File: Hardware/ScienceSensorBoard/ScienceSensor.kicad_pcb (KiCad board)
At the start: 2 copper layers, 96.5 x 94.5 mm, 70 parts, among them J1 RJ45_LED_Shielded, J2 Conn_02x03_Counter_Clockwise, Q1 BSS138, Q2 BSS138, Q3 BSS138, Q4 BSS138, Q5 BSS138, Q6 BSS138, Q7 BSS138, U1 TSR_1-2450, U2 Teensy4.1_DEV-16771

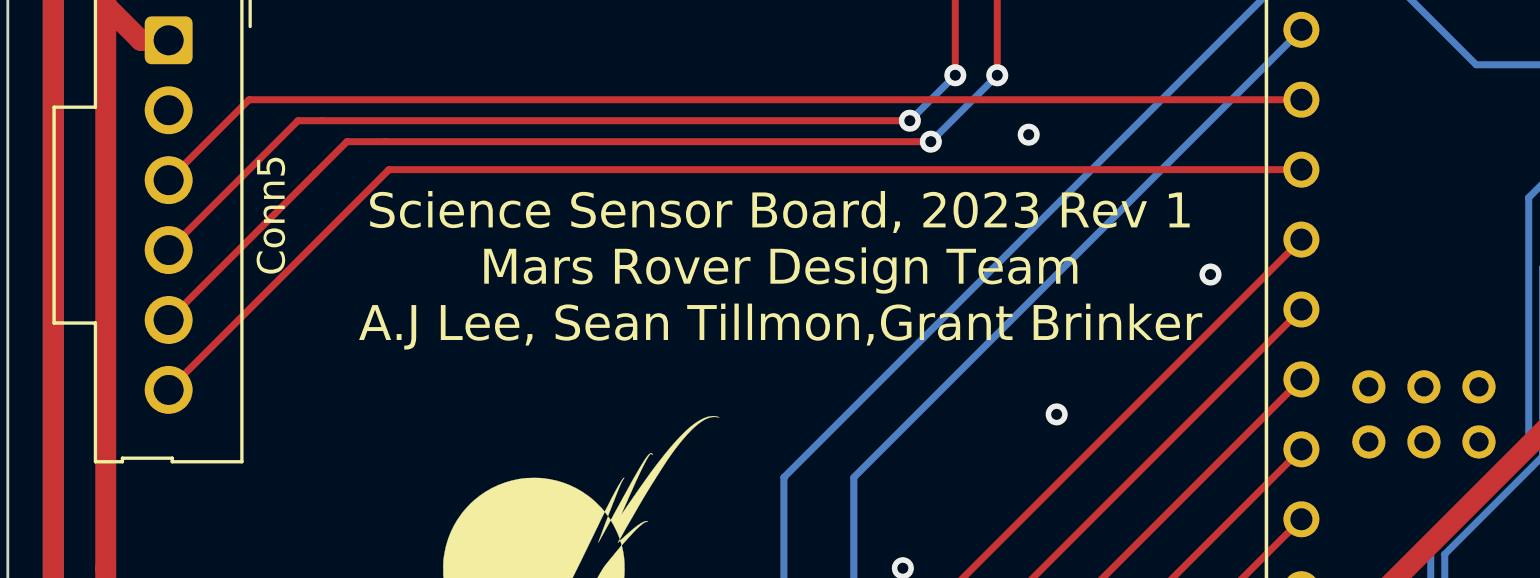
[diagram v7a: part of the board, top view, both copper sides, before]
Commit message: Cleaned up silkscreens
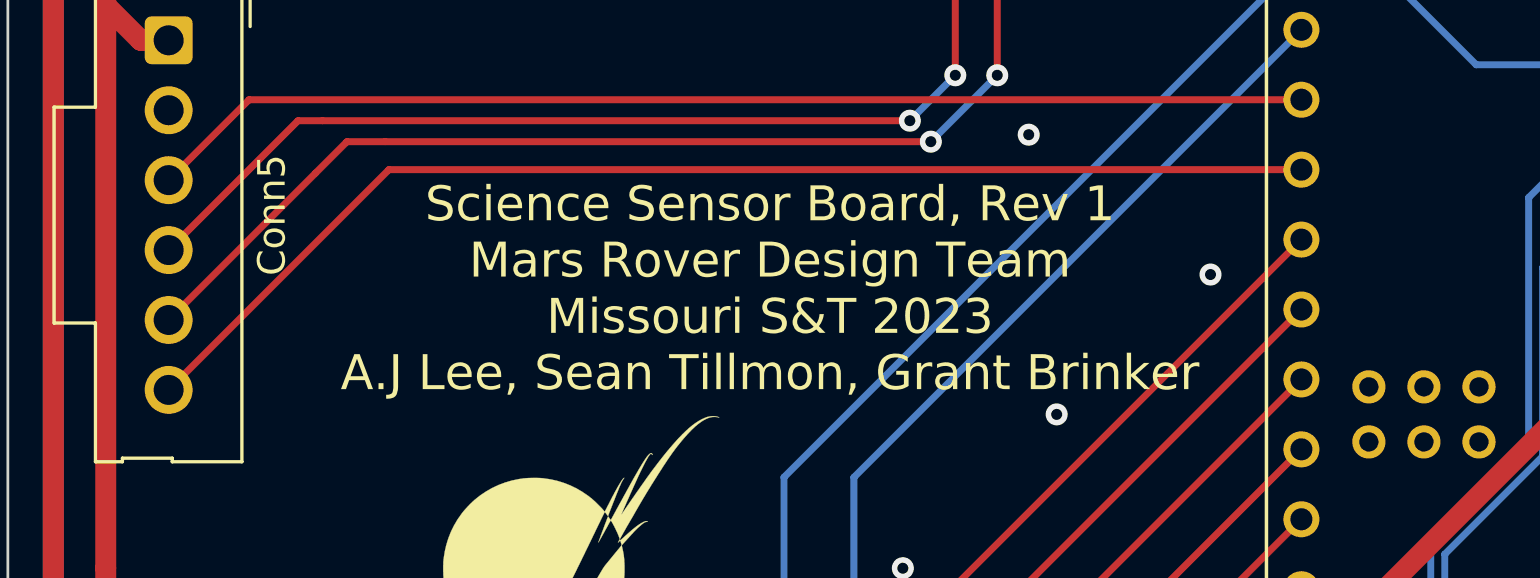
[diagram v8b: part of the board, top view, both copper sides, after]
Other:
- board text added: "Science Sensor Board, Rev 1 Mars Rover Design Team Missouri S&T 2023 A.J Lee, Sean Tillmon, Grant Brinker"
- board text removed: "Science Sensor Board, 2023 Rev 1 Mars Rover Design Team A.J Lee, Sean Tillmon,Grant Brinker"
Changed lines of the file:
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@@
   (gr_arc (start 193.04 137.16) (mid 191.849682 140.033682) (end 188.976 141.224) (layer "Edge.Cuts") (width 0.1))
   (gr_line (start 188.976 141.224) (end 100.584 141.224) (layer "Edge.Cuts") (width 0.1))
-  (gr_text "LEDs" (at 104.394 111.379 270) (layer "B.SilkS")
+  (gr_text "LEDs" (at 106.426 111.379 90) (layer "B.SilkS")
     (effects (font (size 1 1) (thickness 0.15)) (justify mirror))
   )
@@
     (effects (font (size 1 1) (thickness 0.15)) (justify mirror))
   )
-  (gr_text "GND" (at 103.759 69.85 270) (layer "B.SilkS")
-    (effects (font (size 1 1) (thickness 0.15)) (justify mirror))
+  (gr_text "GND" (at 103.759 61.722 270) (layer "B.SilkS")
+    (effects (font (size 1.27 1.27) (thickness 0.15)) (justify mirror))
   )
-  (gr_text "CCD" (at 106.045 87.376 270) (layer "B.SilkS")
+  (gr_text "CCD" (at 106.045 87.376 90) (layer "B.SilkS")
     (effects (font (size 1 1) (thickness 0.15)) (justify mirror))
   )
@@
     (effects (font (size 1 1) (thickness 0.15)) (justify mirror))
   )
-  (gr_text "+ \\ - \\MC\\SH\\ICG\\OS" (at 104.267 87.249 270) (layer "B.SilkS")
+  (gr_text "+ \\ - \\MC\\SH\\ICG\\OS" (at 104.267 87.249 90) (layer "B.SilkS")
     (effects (font (size 1 1) (thickness 0.15)) (justify mirror))
   )
-  (gr_text "12V" (at 103.759 61.976 270) (layer "B.SilkS")
-    (effects (font (size 1 1) (thickness 0.15)) (justify mirror))
+  (gr_text "12V" (at 103.886 69.596 270) (layer "B.SilkS")
+    (effects (font (size 1.27 1.27) (thickness 0.15)) (justify mirror))
   )
-  (gr_text "+ \\ - \\ x \\260\\275\\280\\315" (at 102.362 112.141 270) (layer "B.SilkS")
+  (gr_text "+ \\ - \\ x \\260\\275\\280\\315" (at 104.394 112.141 90) (layer "B.SilkS")
     (effects (font (size 1 1) (thickness 0.15)) (justify mirror))
   )
@@
     (effects (font (size 1.27 1.27) (thickness 0.15)))
   )
-  (gr_text "Science Sensor Board, 2023 Rev 1\nMars Rover Design Team\nA.J Lee, Sean Tillmon,Grant Brinker" (at 124.587 89.154) (layer "F.SilkS")
+  (gr_text "Science Sensor Board, Rev 1\nMars Rover Design Team\nMissouri S&T 2023\nA.J Lee, Sean Tillmon, Grant Brinker" (at 124.206 89.916) (layer "F.SilkS")
     (effects (font (size 1.27 1.27) (thickness 0.15)))
   )
